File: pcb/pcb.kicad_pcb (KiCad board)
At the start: 2 copper layers, 99.9 x 83.3 mm, 128 parts, among them SW1 SW_Push, SW2 SW_Push, SW3 SW_Push

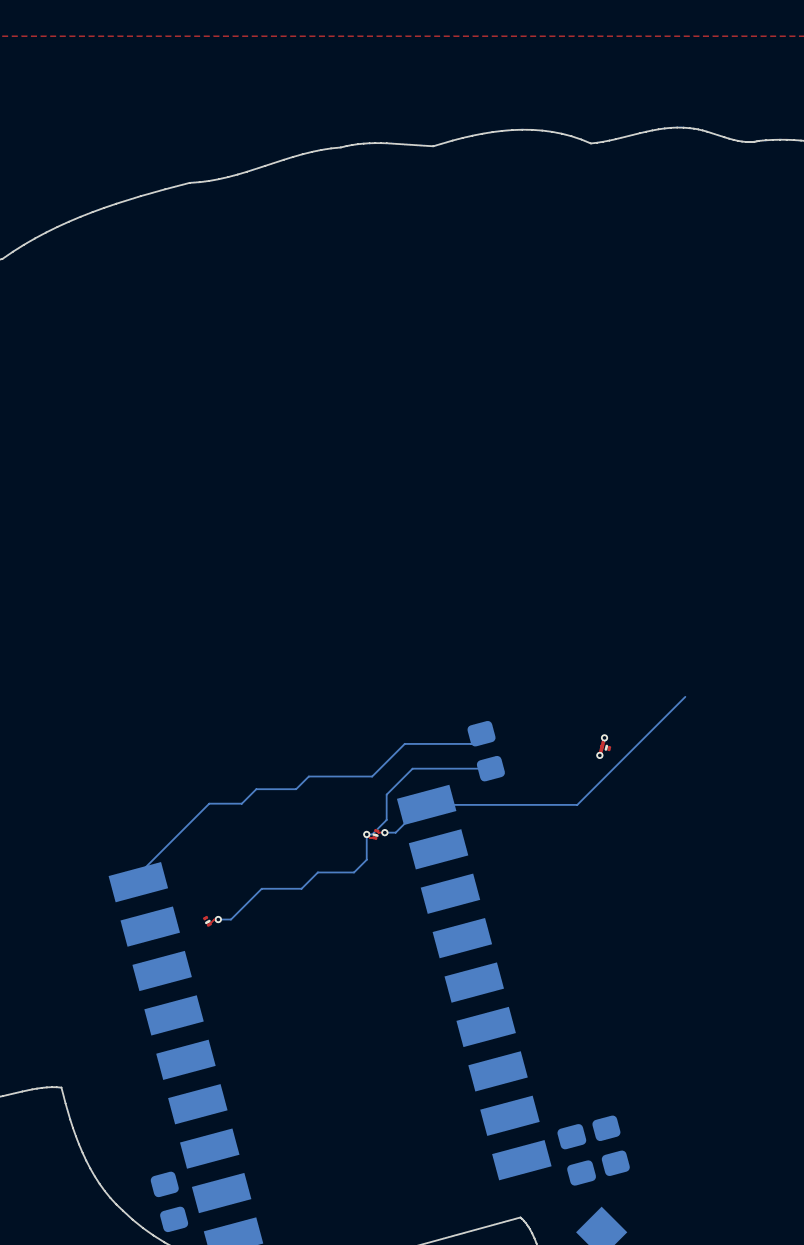
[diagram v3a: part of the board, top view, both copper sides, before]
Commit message: added third keychain hole at the top center
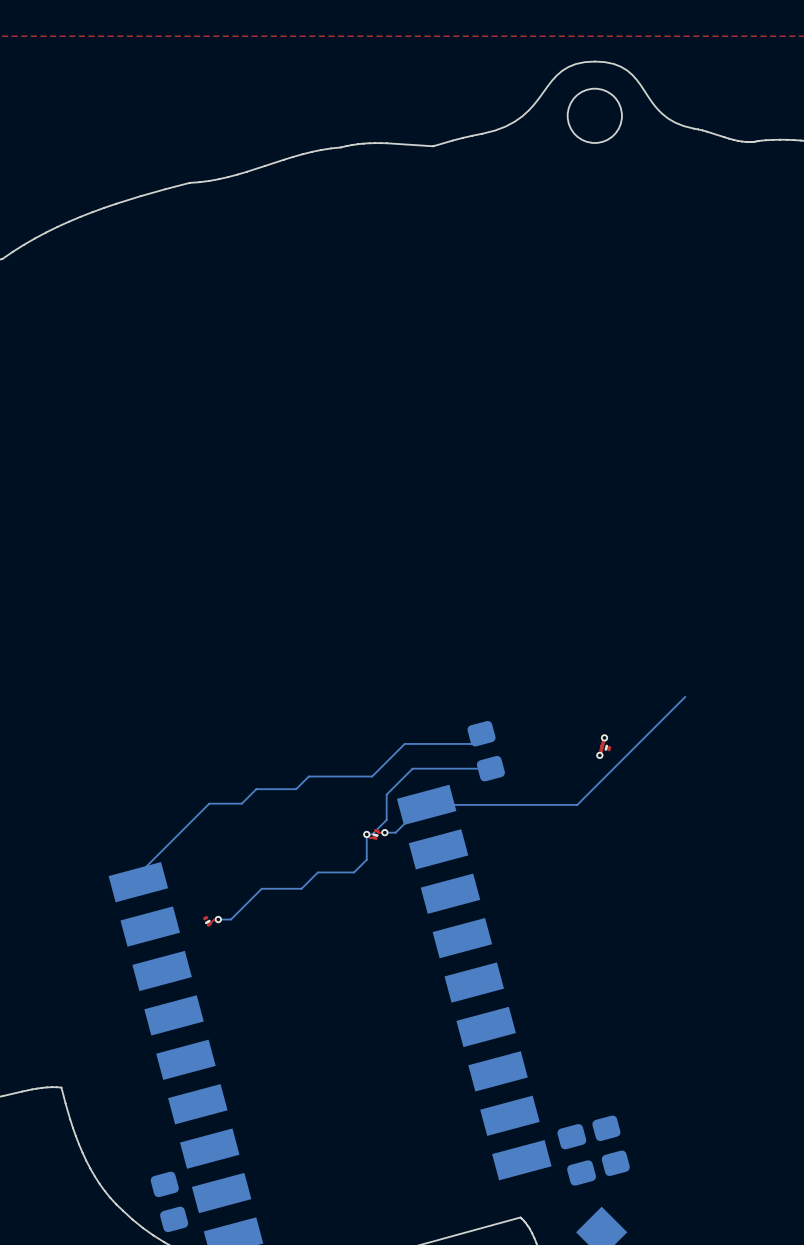
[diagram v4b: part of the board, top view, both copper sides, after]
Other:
- board size 99.9 x 83.3 mm -> 99.9 x 87 mm

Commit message: sorted some lines
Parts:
- turned D21 to -135 degrees
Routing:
- net /Col2: track 50.1 -> 53.8 mm, vias 20 -> 22
- net /Row0: track 27.3 -> 25.7 mm
- net /Col0: track 68.1 -> 66.9 mm
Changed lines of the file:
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@@
 	(footprint "pcb:XL-0201"
 		(layer "F.Cu")
-		(at 131.8 108.9 120)
+		(at 131.8 108.9 -135)
 		(descr "LED SMD 0.7 mm x 0.4 mm, XINGLIGHT XL-0201 series")
 		(tags "LED")
 		(property "Reference" "D21"
-			(at 0 -1.000001 120)
+			(at 0 -1 45)
 			(layer "F.SilkS")
 			(hide yes)
@@
 		)
 		(property "Value" "LED_Small"
-			(at 0 1.000001 120)
+			(at 0 1 45)
 			(layer "F.Fab")
 			(effects
@@
 		)
 		(property "Datasheet" ""
-			(at 0 0 120)
+			(at 0 0 45)
 			(layer "F.Fab")
 			(hide yes)
@@
 		)
 		(property "Description" "Light emitting diode, small symbol"
-			(at 0 0 120)
+			(at 0 0 45)
 			(layer "F.Fab")
 			(hide yes)
@@
 		)
 		(property "KiLib_Generator" "SMD_2terminal_chip_molded"
-			(at 0 0 120)
+			(at 0 0 45)
 			(layer "F.SilkS")
 			(hide yes)
@@
 		)
 		(property "Sim.Pins" "1=K 2=A"
-			(at 0 0 120)
+			(at 0 0 225)
 			(unlocked yes)
 			(layer "F.Fab")
@@
 		)
 		(property "LCSC" "C965789"
-			(at 0 0 120)
+			(at 0 0 225)
 			(unlocked yes)
 			(layer "F.Fab")
@@
 		(duplicate_pad_numbers_are_jumpers no)
 		(fp_line
-			(start -0.039999 -0.099999)
-			(end -0.039998 0.100001)
+			(start -0.04 -0.1)
+			(end -0.039999 0.100001)
 			(stroke
 				(width 0.15)
@@
 		(fp_poly
 			(pts
-				(xy -0.600002 -0.299997) (xy 0.6 -0.3) (xy 0.600002 0.299997) (xy -0.6 0.3)
+				(xy -0.600001 -0.299997) (xy 0.6 -0.3) (xy 0.600001 0.299997) (xy -0.6 0.3)
 			)
 			(stroke
@@
 		(fp_poly
 			(pts
-				(xy -0.325 -0.174998) (xy 0.324998 -0.174999) (xy 0.325 0.174998) (xy -0.324998 0.174999)
+				(xy -0.325 -0.175) (xy 0.325 -0.175) (xy 0.325 0.175) (xy -0.325 0.175)
 			)
 			(stroke
@@
 		)
 		(fp_text user "${REFERENCE}"
-			(at 0 -0.62 120)
+			(at 0 -0.62 45)
 			(layer "F.Fab")
 			(effects
@@
 		)
 		(pad "" smd roundrect
-			(at -0.205 0 120)
+			(at -0.205 0 225)
 			(size 0.15 0.2)
 			(layers "F.Paste")
@@
 		)
 		(pad "" smd roundrect
-			(at 0.205 0 120)
+			(at 0.205 0 225)
 			(size 0.15 0.2)
 			(layers "F.Paste")
@@
 		)
 		(pad "1" smd roundrect
-			(at -0.205 0 120)
+			(at -0.205 0 225)
 			(size 0.17 0.28)
 			(layers "F.Cu" "F.Mask")
@@
 		)
 		(pad "2" smd roundrect
-			(at 0.205 0 120)
+			(at 0.205 0 225)
 			(size 0.17 0.28)
 			(layers "F.Cu" "F.Mask")
@@
 	)
 	(segment
-		(start 132.4 108.8)
-		(end 132.180035 108.8)
-		(width 0.1)
-		(layer "F.Cu")
-		(net "/Row0")
-	)
-	(segment
 		(start 14.098908 161.023168)
 		(end 14.098909 161.518167)
@@
 	)
 	(segment
-		(start 132.180035 108.8)
-		(end 131.9025 109.077535)
+		(start 131.944957 108.755043)
+		(end 132.4 108.565854)
 		(width 0.1)
 		(layer "F.Cu")
@@
 	)
 	(via
-		(at 132.4 108.8)
+		(at 132.4 108.565854)
 		(size 0.4)
 		(drill 0.2)
@@
 	)
 	(segment
-		(start 141.7 101.9)
-		(end 141.7 103.3)
-		(width 0.1)
-		(layer "B.Cu")
-		(net "/Row0")
-	)
-	(segment
-		(start 133.1 108.8)
-		(end 132.4 108.8)
-		(width 0.1)
-		(layer "B.Cu")
-		(net "/Row0")
-	)
-	(segment
-		(start 137.9 106.2)
-		(end 137 107.1)
+		(start 141.9 101.7)
+		(end 147.458819 100.465926)
 		(width 0.1)
 		(layer "B.Cu")
@@
 	)
 	(segment
-		(start 141.7 103.3)
-		(end 140.9 104.1)
-		(width 0.1)
-		(layer "B.Cu")
-		(net "/Row0")
-	)
-	(segment
-		(start 134.8 107.1)
-		(end 133.1 108.8)
-		(width 0.1)
-		(layer "B.Cu")
-		(net "/Row0")
-	)
-	(segment
-		(start 140.6 105.5)
-		(end 139.9 106.2)
-		(width 0.1)
-		(layer "B.Cu")
-		(net "/Row0")
-	)
-	(segment
-		(start 137 107.1)
-		(end 134.8 107.1)
+		(start 140.6 104.1)
+		(end 141.9 101.7)
 		(width 0.1)
 		(layer "B.Cu")
@@
 	)
 	(segment
-		(start 140.9 104.1)
-		(end 140.6 104.1)
+		(start 132.4 108.565854)
+		(end 140.5 105.8)
 		(width 0.1)
 		(layer "B.Cu")
@@
 	)
 	(segment
-		(start 143.134074 100.465926)
-		(end 141.7 101.9)
-		(width 0.1)
-		(layer "B.Cu")
-		(net "/Row0")
-	)
-	(segment
-		(start 147.458819 100.465926)
-		(end 143.134074 100.465926)
-		(width 0.1)
-		(layer "B.Cu")
-		(net "/Row0")
-	)
-	(segment
-		(start 139.9 106.2)
-		(end 137.9 106.2)
-		(width 0.1)
-		(layer "B.Cu")
-		(net "/Row0")
-	)
-	(segment
-		(start 140.6 104.1)
-		(end 140.6 105.5)
+		(start 140.5 105.8)
+		(end 140.6 104.1)
 		(width 0.1)
 		(layer "B.Cu")
@@
 	)
 	(segment
-		(start 141.6 104)
-		(end 142.2 104)
-		(width 0.1)
+		(start 34.598908 160.618167)
+		(end 38.598909 160.618166)
+		(width 0.2)
 		(layer "B.Cu")
 		(net "/Col1")
 	)
 	(segment
-		(start 34.598908 160.618167)
-		(end 38.598909 160.618166)
-		(width 0.2)
+		(start 141.6 104)
+		(end 143.909876 102.467974)
+		(width 0.1)
 		(layer "B.Cu")
 		(net "/Col1")
@@
 	)
 	(segment
-		(start 142.2 104)
-		(end 143.732024 102.467976)
-		(width 0.1)
-		(layer "B.Cu")
-		(net "/Col1")
-	)
-	(segment
 		(start 39.598909 160.618166)
 		(end 43.598908 160.618165)
@@
 	)
 	(segment
-		(start 131.9 102.4)
-		(end 133.7 102.4)
-		(width 0.1)
-		(layer "B.Cu")
-		(net "/Col0")
-	)
-	(segment
 		(start 44.598909 165.618167)
 		(end 48.598909 165.618167)
@@
 	)
 	(segment
-		(start 133.7 102.4)
-		(end 134.5 101.6)
-		(width 0.1)
-		(layer "B.Cu")
-		(net "/Col0")
-	)
-	(segment
-		(start 127.981754 106.735899)
-		(end 127.981754 106.318246)
-		(width 0.1)
+		(start 59.598908 165.618168)
+		(end 63.598909 165.618166)
+		(width 0.2)
 		(layer "B.Cu")
 		(net "/Col0")
 	)
 	(segment
-		(start 146.375255 99.1)
-		(end 146.941181 98.534074)
+		(start 127.981759 106.7359)
+		(end 131.1 102.9)
 		(width 0.1)
 		(layer "B.Cu")
@@
 	)
 	(segment
-		(start 59.598908 165.618168)
-		(end 63.598909 165.618166)
-		(width 0.2)
-		(layer "B.Cu")
-		(net "/Col0")
-	)
-	(segment
 		(start 34.598908 165.618167)
 		(end 38.598908 165.618168)
@@
 	)
 	(segment
-		(start 137.4 100.9)
-		(end 140.9 100.9)
-		(width 0.1)
-		(layer "B.Cu")
-		(net "/Col0")
-	)
-	(segment
-		(start 127.981754 106.318246)
-		(end 131.9 102.4)
-		(width 0.1)
-		(layer "B.Cu")
-		(net "/Col0")
-	)
-	(segment
 		(start 29.598908 165.618166)
 		(end 33.598908 165.618168)
@@
 	)
 	(segment
-		(start 134.5 101.6)
-		(end 136.7 101.6)
-		(width 0.1)
-		(layer "B.Cu")
-		(net "/Col0")
-	)
-	(segment
-		(start 142.7 99.1)
-		(end 146.375255 99.1)
-		(width 0.1)
-		(layer "B.Cu")
-		(net "/Col0")
-	)
-	(segment
 		(start 19.598908 165.618165)
 		(end 23.59891 165.618167)
@@
 	)
 	(segment
-		(start 140.9 100.9)
-		(end 142.7 99.1)
-		(width 0.1)
-		(layer "B.Cu")
-		(net "/Col0")
-	)
-	(segment
 		(start 39.598908 165.618166)
 		(end 43.598909 165.618166)
@@
 	)
 	(segment
-		(start 136.7 101.6)
-		(end 137.4 100.9)
+		(start 131.1 102.9)
+		(end 146.941181 98.534074)
 		(width 0.1)
 		(layer "B.Cu")
@@
 	)
 	(segment
+		(start 131.655043 109.044957)
+		(end 132.2 109.3)
+		(width 0.1)
+		(layer "F.Cu")
+		(net "/Col2")
+	)
+	(segment
 		(start 59.103909 155.618166)
 		(end 59.098908 155.613166)
@@
 	)
 	(segment
+		(start 131.1 108.911299)
+		(end 131.655043 109.044957)
+		(width 0.1)
+		(layer "F.Cu")
+		(net "/Col2")
+	)
+	(segment
 		(start 54.098908 155.613166)
 		(end 54.093909 155.618167)
@@
 	)
 	(via
+		(at 131.1 108.911299)
+		(size 0.4)
+		(drill 0.2)
+		(layers "F.Cu" "B.Cu")
+		(net "/Col2")
+	)
+	(via
 		(at 23.598909 155.618166)
 		(size 0.4)
@@
 	)
 	(via
+		(at 132.2 109.3)
+		(size 0.4)
+		(drill 0.2)
+		(layers "F.Cu" "B.Cu")
+		(net "/Col2")
+	)
+	(via
 		(at 53.598908 155.618167)
 		(size 0.4)
@@
 		(layer "B.Cu")
 		(net "/Col2")
+	)
+	(segment
+		(start 128.639159 109.189351)
+		(end 131.1 108.911299)
+		(width 0.1)
+		(layer "B.Cu")
+		(net "/Col2")
